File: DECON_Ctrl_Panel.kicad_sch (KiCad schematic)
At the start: 0 parts

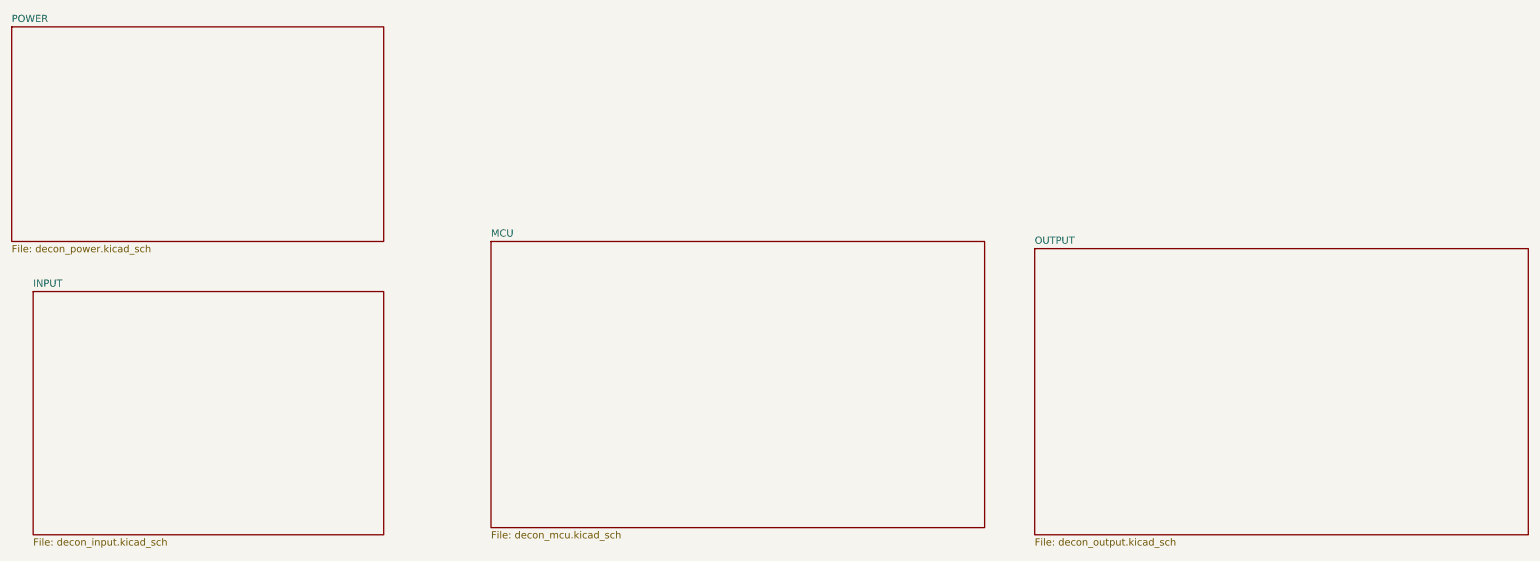
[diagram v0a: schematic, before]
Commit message: modified:   DECON_Ctrl_Panel.kicad_sch
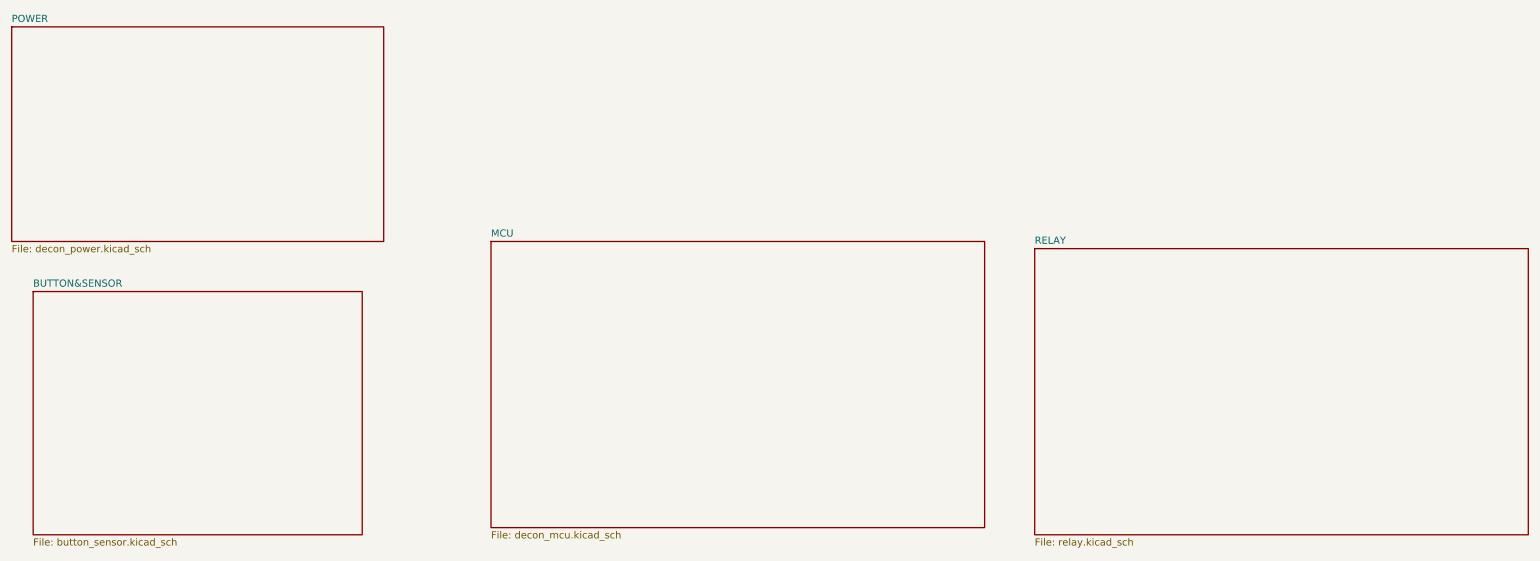
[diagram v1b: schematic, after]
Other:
- sheet INPUT renamed BUTTON&SENSOR
- sheet OUTPUT renamed RELAY
- sheet BUTTON&SENSOR: file decon_input.kicad_sch -> button_sensor.kicad_sch
- sheet RELAY: file decon_output.kicad_sch -> relay.kicad_sch
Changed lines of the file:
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@@
 	(sheet
 		(at 85.09 78.74)
-		(size 62.23 43.18)
+		(size 58.42 43.18)
 		(exclude_from_sim no)
 		(in_bom yes)
@@
 			(color 0 0 0 0.0000)
 		)
-		(property "Sheetname" "INPUT"
+		(property "Sheetname" "BUTTON&SENSOR"
 			(at 85.09 78.0284 0)
 			(effects
@@
 			)
 		)
-		(property "Sheetfile" "decon_input.kicad_sch"
+		(property "Sheetfile" "button_sensor.kicad_sch"
 			(at 85.09 122.5046 0)
 			(effects
@@
 			(color 0 0 0 0.0000)
 		)
-		(property "Sheetname" "OUTPUT"
+		(property "Sheetname" "RELAY"
 			(at 262.89 70.4084 0)
 			(effects
@@
 			)
 		)
-		(property "Sheetfile" "decon_output.kicad_sch"
+		(property "Sheetfile" "relay.kicad_sch"
 			(at 262.89 122.5046 0)
 			(effects

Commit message: new file:   decon_ctrl.pdf
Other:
- removed sheet POWER
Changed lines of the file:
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@@
-		)
-	)
-	(sheet
-		(at 81.28 31.75)
-		(size 66.04 38.1)
-		(exclude_from_sim no)
-		(in_bom yes)
-		(on_board yes)
-		(dnp no)
-		(fields_autoplaced yes)
-		(stroke
-			(width 0.1524)
-			(type solid)
-		)
-		(fill
-			(color 0 0 0 0.0000)
-		)
-		(property "Sheetname" "POWER"
-			(at 81.28 31.0384 0)
-			(effects
-				(font
-					(size 1.27 1.27)
-				)
-				(justify left bottom)
-			)
-		)
-		(property "Sheetfile" "decon_power.kicad_sch"
-			(at 81.28 70.4346 0)
-			(effects
-				(font
-					(size 1.27 1.27)
-				)
-				(justify left top)
-			)
-		)
-		(instances
-			(project "DECON_Ctrl_Panel"
-				(path "/47267b0b-286c-4b8f-b9a8-0ba7bc68aaf0"
-					(page "5")
-				)
-			)
 		)
 	)
